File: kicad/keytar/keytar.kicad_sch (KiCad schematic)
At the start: 12 parts, among them J1 , J2 USB_B, J3 AudioJack2, J4 Conn_01x04, J5 USB_A, J6 Mini-DIN-6, U1 Pico

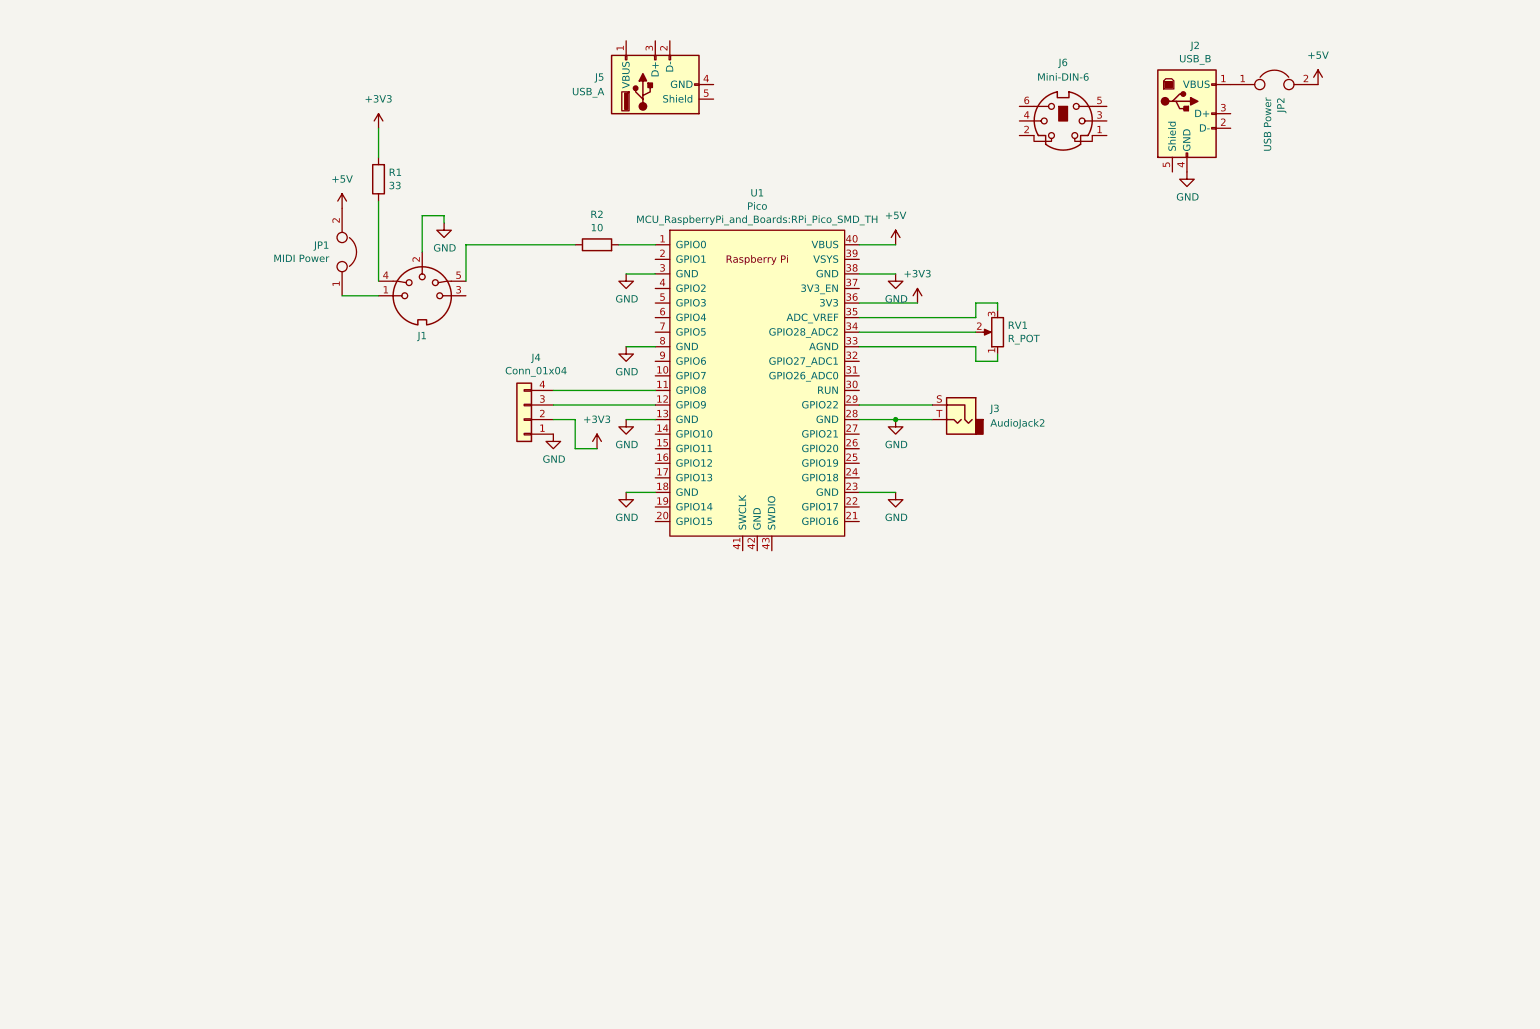
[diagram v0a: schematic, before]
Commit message: shrink PCB, add USB and PS/2 ports
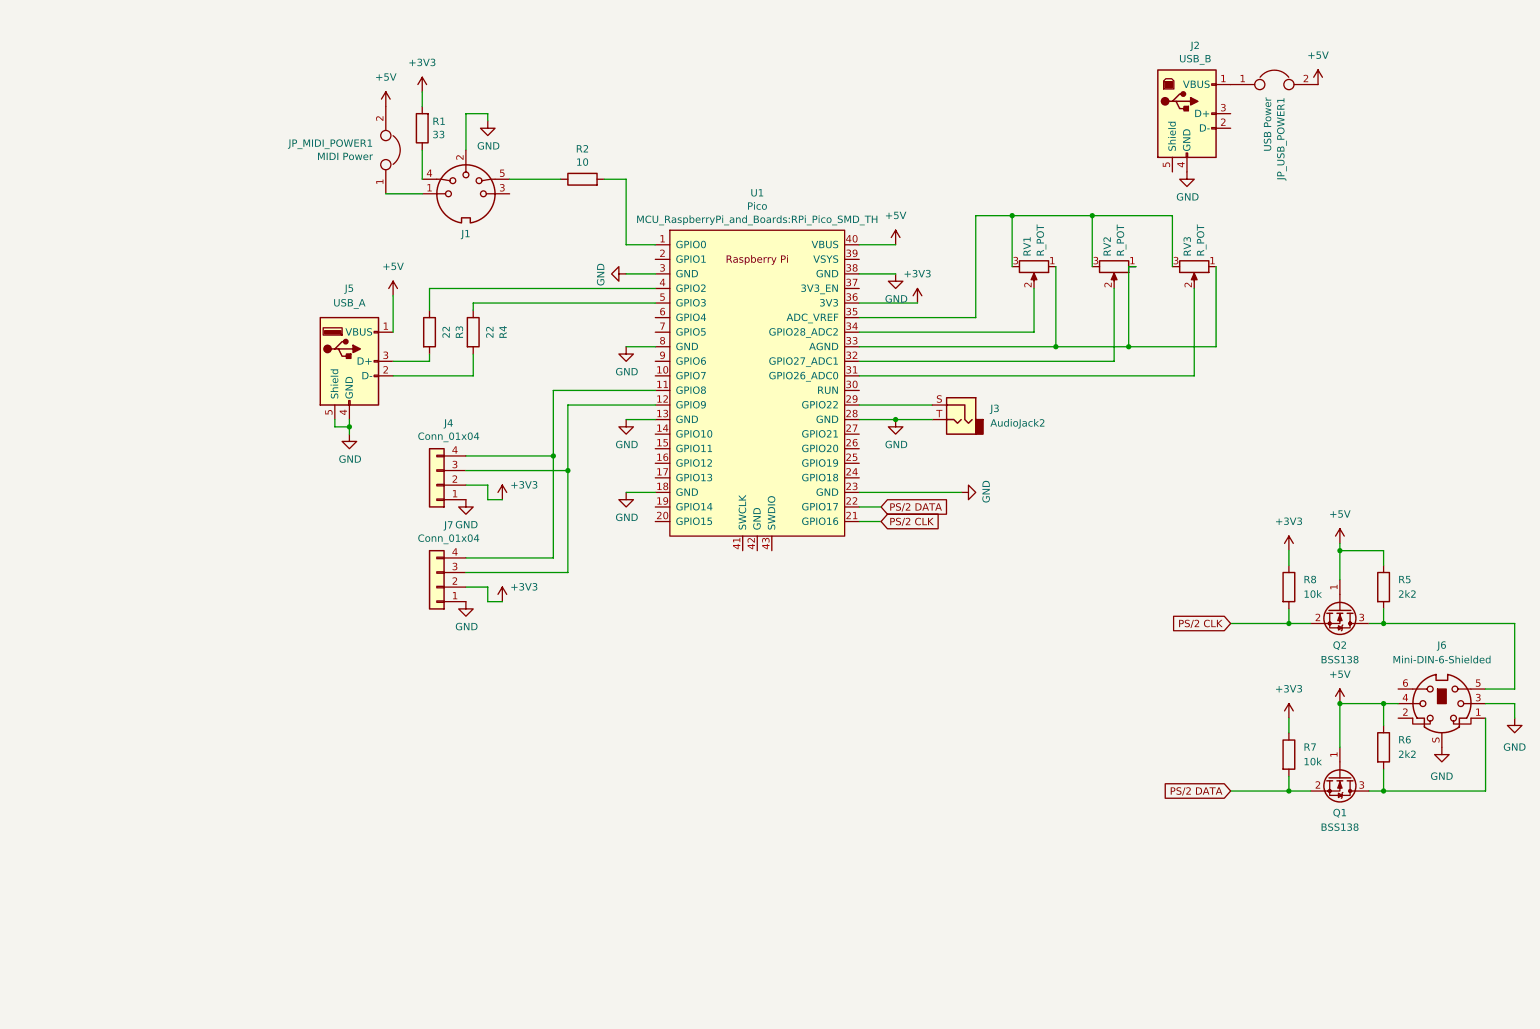
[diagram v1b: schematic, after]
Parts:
- removed J6: Mini-DIN-6, symbol Connector:Mini-DIN-6
- added J6: Mini-DIN-6-Shielded, keyar-parts:EB-DIOS M06, symbol keytar-parts:Mini-DIN-6-Shielded
- added J7: Conn_01x04, Connector_JST:JST_XH_B4B-XH-A_1x04_P2.50mm_Vertical, symbol Connector_Generic:Conn_01x04
- added Q1, Q2: BSS138, Package_TO_SOT_SMD:SOT-23, symbol Transistor_FET:BSS138
- added R3, R4: 22, Resistor_SMD:R_1206_3216Metric_Pad1.30x1.75mm_HandSolder, symbol Device:R
- added R5, R6: 2k2, Resistor_SMD:R_1206_3216Metric_Pad1.30x1.75mm_HandSolder, symbol Device:R
- added R7, R8: 10k, Resistor_SMD:R_1206_3216Metric_Pad1.30x1.75mm_HandSolder, symbol Device:R
- added RV2, RV3: R_POT, Connector_JST:JST_XH_B3B-XH-A_1x03_P2.50mm_Vertical, symbol keytar-rescue:R_POT-Device
- renumbered JP1 to JP_MIDI_POWER1, JP2 to JP_USB_POWER1
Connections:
- net +3V3: now also J7.2 (Pin_2), R7.1, R8.1
- net +5V: now also J5.1 (VBUS), J6.4, Q1.1 (G), Q2.1 (G), R5.1, R6.1
- net GND: now also J5.4 (GND), J5.5 (Shield), J6.3, J6.S, J7.1 (Pin_1)
- net at J4.4 (Pin_4), U1.11 (GPIO8): now also J7.4 (Pin_4)
- net at J4.3 (Pin_3), U1.12 (GPIO9): now also J7.3 (Pin_3)
- net PS/2 CLK: now reaches U1.21 (GPIO16)
- net PS/2 CLK: now also Q2.2 (S), R8.2
- net PS/2 DATA: now reaches U1.22 (GPIO17)
- net PS/2 DATA: now also Q1.2 (S), R7.2
- net at U1.31 (GPIO26_ADC0): now also RV3.2
- net at U1.32 (GPIO27_ADC1): now also RV2.2
- net at RV1.1, U1.33 (AGND): now also RV2.1, RV3.1
- net at RV1.3, U1.35 (ADC_VREF): now also RV2.3, RV3.3
- net at U1.4 (GPIO2): now also R3.1
- net at U1.5 (GPIO3): now also R4.1
- net at J5.2 (D-): now also R4.2
- net at J5.3 (D+): now also R3.2
- new net: J6.5, Q2.3 (D), R5.2
- new net: J6.1, Q1.3 (D), R6.2
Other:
- moved on the sheet: J1, J4, J5, JP_MIDI_POWER1, R1, R2, RV1

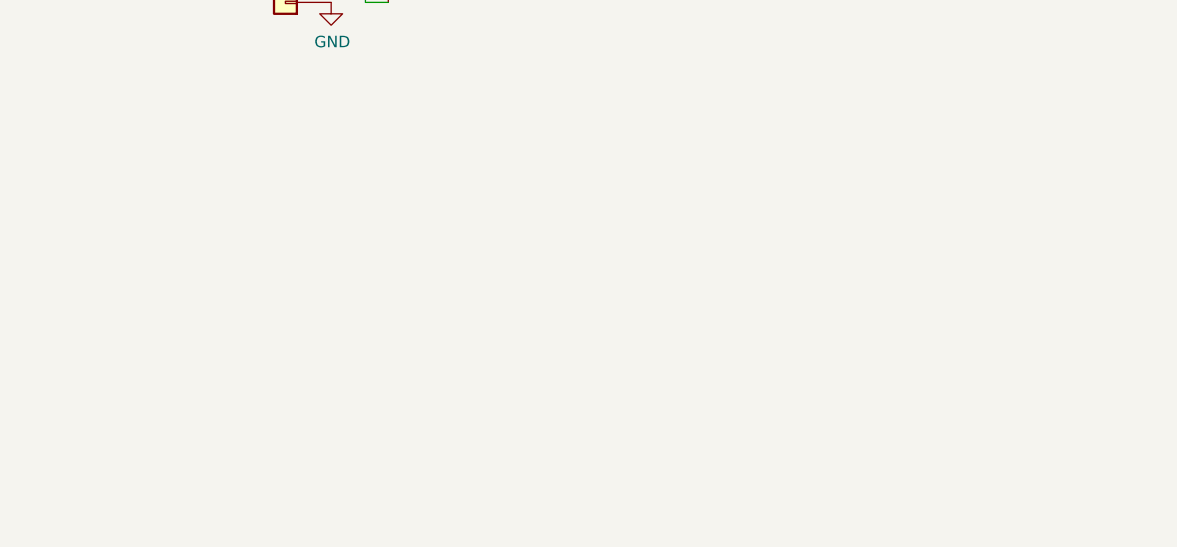
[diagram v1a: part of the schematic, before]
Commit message: add battery management
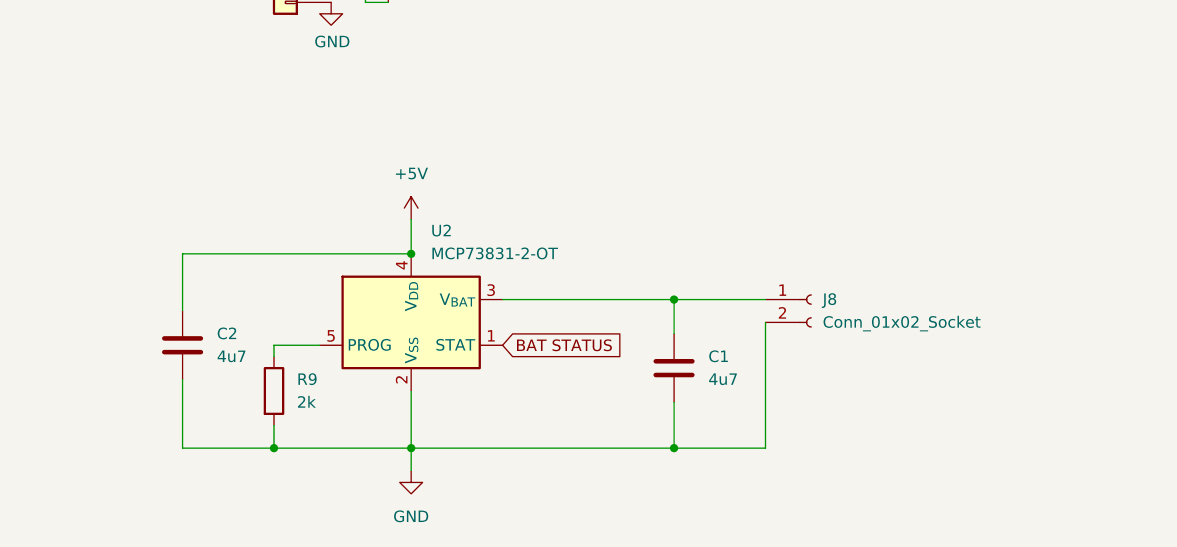
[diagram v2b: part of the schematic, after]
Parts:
- added C1, C2: 4u7, Capacitor_SMD:C_1206_3216Metric_Pad1.33x1.80mm_HandSolder, symbol Device:C
- added J8: Conn_01x02_Socket, symbol Connector:Conn_01x02_Socket
- added R9: 2k, Resistor_SMD:R_1206_3216Metric_Pad1.30x1.75mm_HandSolder, symbol Device:R
- added U2: MCP73831-2-OT, Package_TO_SOT_SMD:SOT-23-5, symbol Battery_Management:MCP73831-2-OT
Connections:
- net +5V: now also C2.1, U2.4 (V_{DD})
- net GND: now also C1.2, C2.2, J8.2 (Pin_2), R9.2, U2.2 (V_{SS})
- new net: C1.1, J8.1 (Pin_1), U2.3 (V_{BAT})
- new net: R9.1, U2.5 (PROG)
- new net BAT STATUS: U2.1 (STAT)

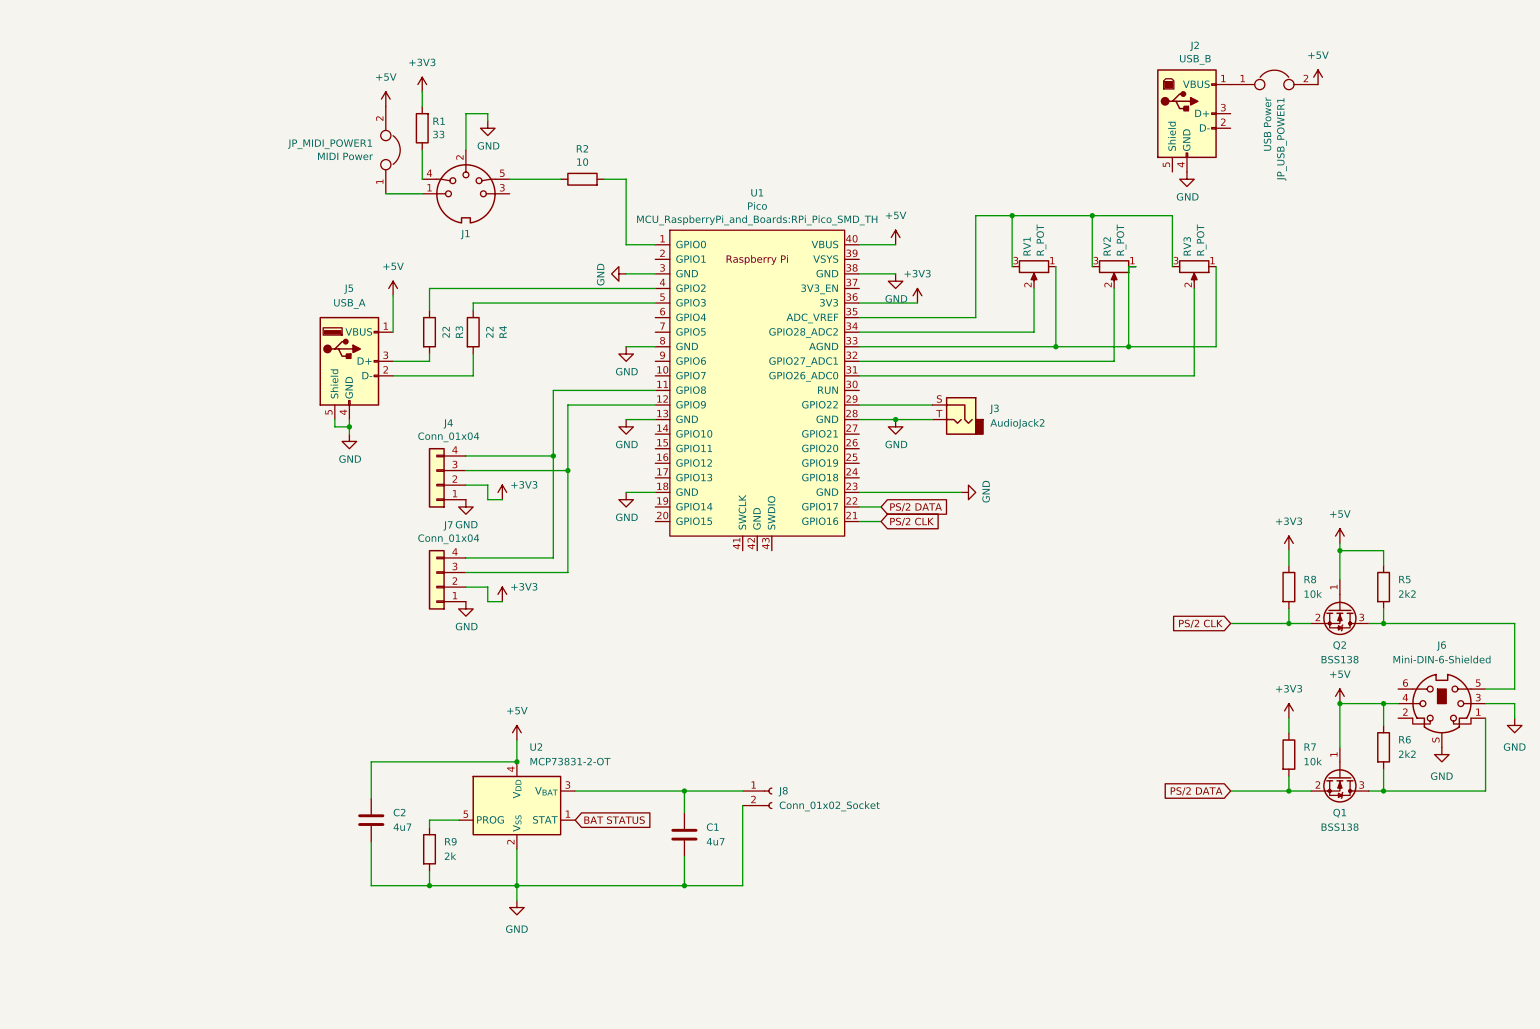
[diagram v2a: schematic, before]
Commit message: adjust midi pin
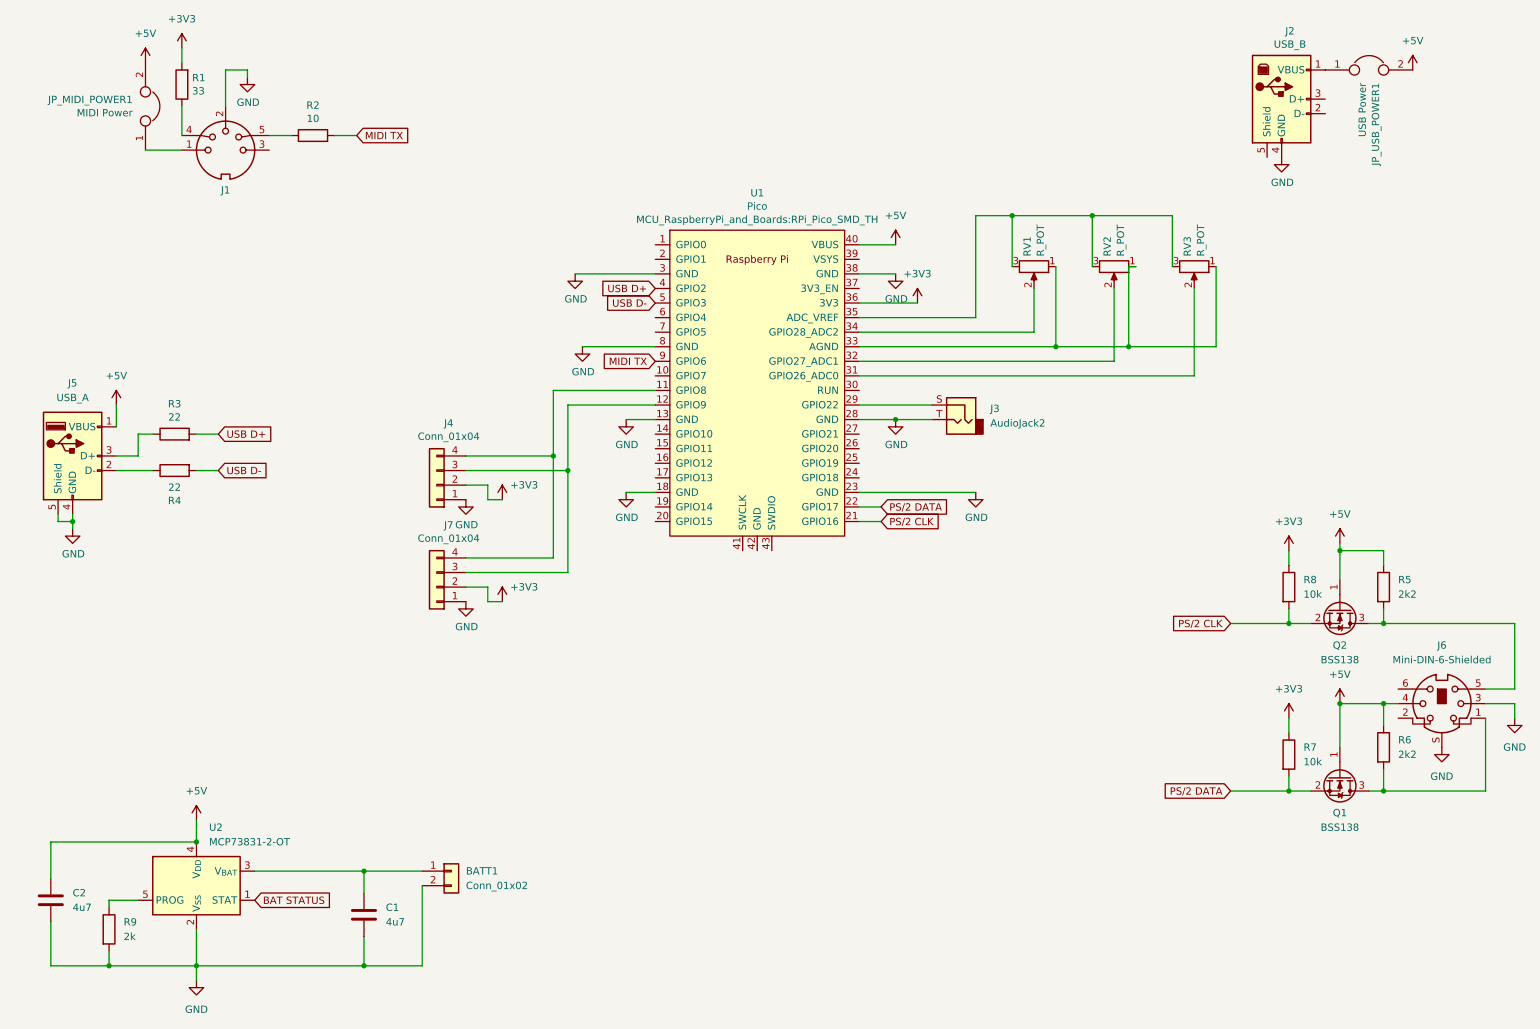
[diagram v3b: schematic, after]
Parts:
- removed J8: Conn_01x02_Socket, symbol Connector:Conn_01x02_Socket
- added BATT1: Conn_01x02, Connector_JST:JST_XH_B2B-XH-A_1x02_P2.50mm_Vertical, symbol Connector_Generic:Conn_01x02
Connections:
- net GND: now also BATT1.2 (Pin_2)
- net at U1.1 (GPIO0): no longer R2.2
- net at R3.1: now also J5.3 (D+); no longer U1.4 (GPIO2)
- net at R4.1: now also J5.2 (D-); no longer U1.5 (GPIO3)
- net MIDI TX: now reaches U1.9 (GPIO6)
- net MIDI TX: now also R2.2
- net USB D-: now reaches R4.2
- net USB D-: now also U1.5 (GPIO3); no longer J5.2 (D-)
- net at C1.1, U2.3 (V_{BAT}): now also BATT1.1 (Pin_1)
- net USB D+: now reaches R3.2
- net USB D+: now also U1.4 (GPIO2); no longer J5.3 (D+)
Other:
- moved on the sheet: C1, C2, J1, J2, J5, JP_MIDI_POWER1, JP_USB_POWER1, R1, R2, R3, R4, R9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

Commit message: route board
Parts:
- removed JP_MIDI_POWER1: MIDI Power, Connector_PinHeader_2.54mm:PinHeader_1x02_P2.54mm_Vertical, symbol keytar-rescue:Jumper-Device
- removed JP_USB_POWER1: USB Power, Connector_PinHeader_2.54mm:PinHeader_1x02_P2.54mm_Vertical, symbol keytar-rescue:Jumper-Device
- removed U2: MCP73831-2-OT, Package_TO_SOT_SMD:SOT-23-5, symbol Battery_Management:MCP73831-2-OT
- added C3: 22u, Capacitor_SMD:C_1206_3216Metric_Pad1.33x1.80mm_HandSolder, symbol Device:C
- added D1, D2, D3: D_Schottky, Diode_SMD:D_SMA, symbol Device:D_Schottky
- added L1: 22u, Inductor_SMD:L_Bourns-SRN4018, symbol Device:L
- added R10: 1k, Resistor_SMD:R_1206_3216Metric_Pad1.30x1.75mm_HandSolder, symbol Device:R
- added R11: 7k5, Resistor_SMD:R_1206_3216Metric_Pad1.30x1.75mm_HandSolder, symbol Device:R
- added SW1: SW_DPST_x2, symbol Switch:SW_DPST_x2
- added U2: ~, Package_SO:HSOP-8-1EP_3.9x4.9mm_P1.27mm_EP2.3x2.3mm_ThermalVias, symbol keytar-parts:TP4056
- added U3: MT3608, Package_TO_SOT_SMD:SOT-23-6, symbol Regulator_Switching:MT3608
- C1: value 4u7 -> 22u
- C2: value 4u7 -> 10u
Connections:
- net +3V3: now also RV1.3, RV2.3, RV3.3
- net +5V: now also C3.1, D1.1 (K), R11.2; no longer C2.1
- net GND: now also J3.S, RV1.1, RV2.1, RV3.1, C3.2, R10.2, U2.1 (TEMP), U2.3 (GND), U2.9 (HEATSINK), U3.2 (GND); no longer J3.T
- net at U1.29 (GPIO22): no longer J3.S
- net PEDAL: now reaches U1.6 (GPIO4)
- net PEDAL: now also J3.T
- net at J2.1 (VBUS): now also D3.2 (A)
- net at J1.1: now also D2.2 (A)
- net +BATT: now reaches BATT1.1 (Pin_1), C1.1
- net +BATT: now also SW1.1 (A), U2.5 (BAT)
- net at R9.1: now also U2.2 (PROG)
- new net: L1.1, SW1.2 (B), U3.4 (EN), U3.5 (IN)
- new net: D1.2 (A), L1.2, U3.1 (SW)
- new net: R10.1, R11.1, U3.3 (FB)
- new net VBUS: C2.1, D2.1 (K), D3.1 (K), U2.4 (VCC), U2.8 (CE)
- now unconnected: U1.33 (AGND), U1.35 (ADC_VREF)
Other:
- moved on the sheet: BATT1, C1, C2, J3, R3, R4

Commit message: improve pcb
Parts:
- added J_NO_BATT1: Jumper_2_Open, Jumper:SolderJumper-2_P1.3mm_Open_RoundedPad1.0x1.5mm, symbol Jumper:Jumper_2_Open
- SW1: footprint (none) -> Connector_JST:JST_XH_B3B-XH-A_1x03_P2.50mm_Vertical
- U1: footprint MCU_RaspberryPi_and_Boards:RPi_Pico_SMD_TH -> keyar-parts:RPi_Pico_debug_hole_USB_SMD_TH; symbol keytar-rescue:Pico-MCU_RaspberryPi_and_Boards -> keytar-parts:Pico_USB
- U2: footprint Package_SO:HSOP-8-1EP_3.9x4.9mm_P1.27mm_EP2.3x2.3mm_ThermalVias -> Package_SO:HSOP-8-1EP_3.9x4.9mm_P1.27mm_EP2.3x2.3mm
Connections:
- net +5V: now also J_NO_BATT1.2 (B)
- net GND: now also J2.5 (Shield)
- net VBUS: now also J_NO_BATT1.1 (A)
- net 5V_USB: now reaches D3.2 (A), J2.1 (VBUS)
- net USB DEV D-: now reaches J2.2 (D-)
- net USB DEV D-: now also U1.44 (TP2_D-)
- net USB DEV D+: now reaches J2.3 (D+)
- net USB DEV D+: now also U1.45 (TP3_D+)
- net 5V_MIDI: now reaches D2.2 (A), J1.1
- net REG_IN: now reaches L1.1, SW1.2 (B), U3.4 (EN), U3.5 (IN)
- net REG_OUT: now reaches D1.2 (A), L1.2, U3.1 (SW)
- net USB D+ renamed USB HOST D+
- net USB D- renamed USB HOST D-
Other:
- moved on the sheet: D3
